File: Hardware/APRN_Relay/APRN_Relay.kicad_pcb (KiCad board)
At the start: 2 copper layers, 64 x 56 mm, 31 parts, among them J101 Pi_Zero, J102 SERVO1, J103 SERVO2, J104 PTT, J105 RADIO, J106 CHG_IN, U101 DHT11, U102 NCV1117ST50T3G

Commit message: Add text to the front (and ID for JLCPCB)
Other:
- board text added: "APRN Relay Board KW1FOX ${FULL_REVISION}"
- board text added: "JLCJLCJLCJLC"
- board text removed: "APRN Relay Board ${FULL_REVISION}"
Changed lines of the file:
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@@
   (gr_arc (start 100 153) (mid 97.87868 152.12132) (end 97 150) (layer "Edge.Cuts") (width 0.1))
   (gr_arc (start 161 150) (mid 160.12132 152.12132) (end 158 153) (layer "Edge.Cuts") (width 0.1))
-  (gr_text "APRN Relay Board\n${FULL_REVISION}" (at 100 136.5 90) (layer "F.SilkS")
-    (effects (font (size 1.5 1.5) (thickness 0.3)))
+  (gr_text "APRN Relay Board\nKW1FOX\n${FULL_REVISION}" (at 100.5 146.75 90) (layer "F.SilkS")
+    (effects (font (size 1.3 1.5) (thickness 0.3)) (justify left))
+  )
+  (gr_text "JLCJLCJLCJLC" (at 104.5 140.25 90) (layer "F.SilkS")
+    (effects (font (size 0.9 0.7) (thickness 0.175)))
   )
   (segment (start 142 151.515) (end 137 151.515) (width 0.4) (layer "F.Cu") (net 1))

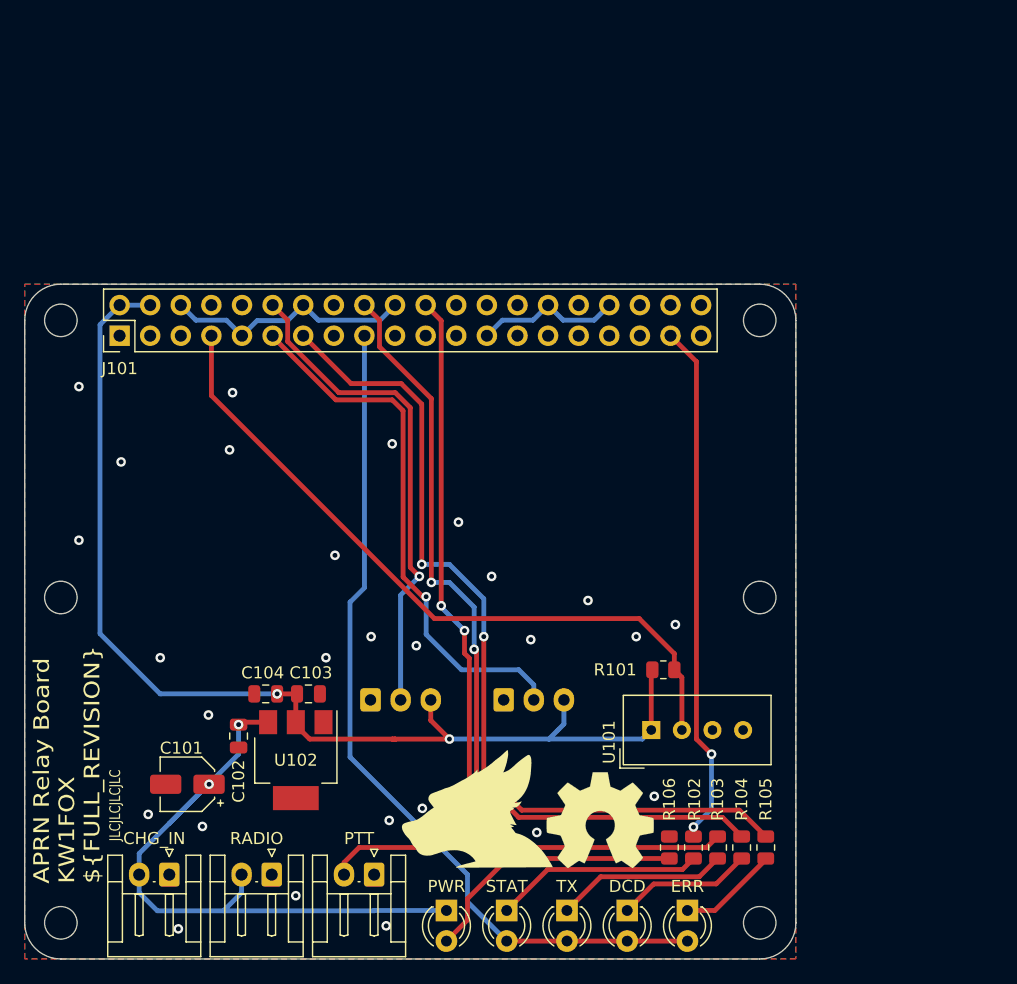
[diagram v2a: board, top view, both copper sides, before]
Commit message: Clean the last bits and prep for a tidy final review series, merge into 1.0 when done
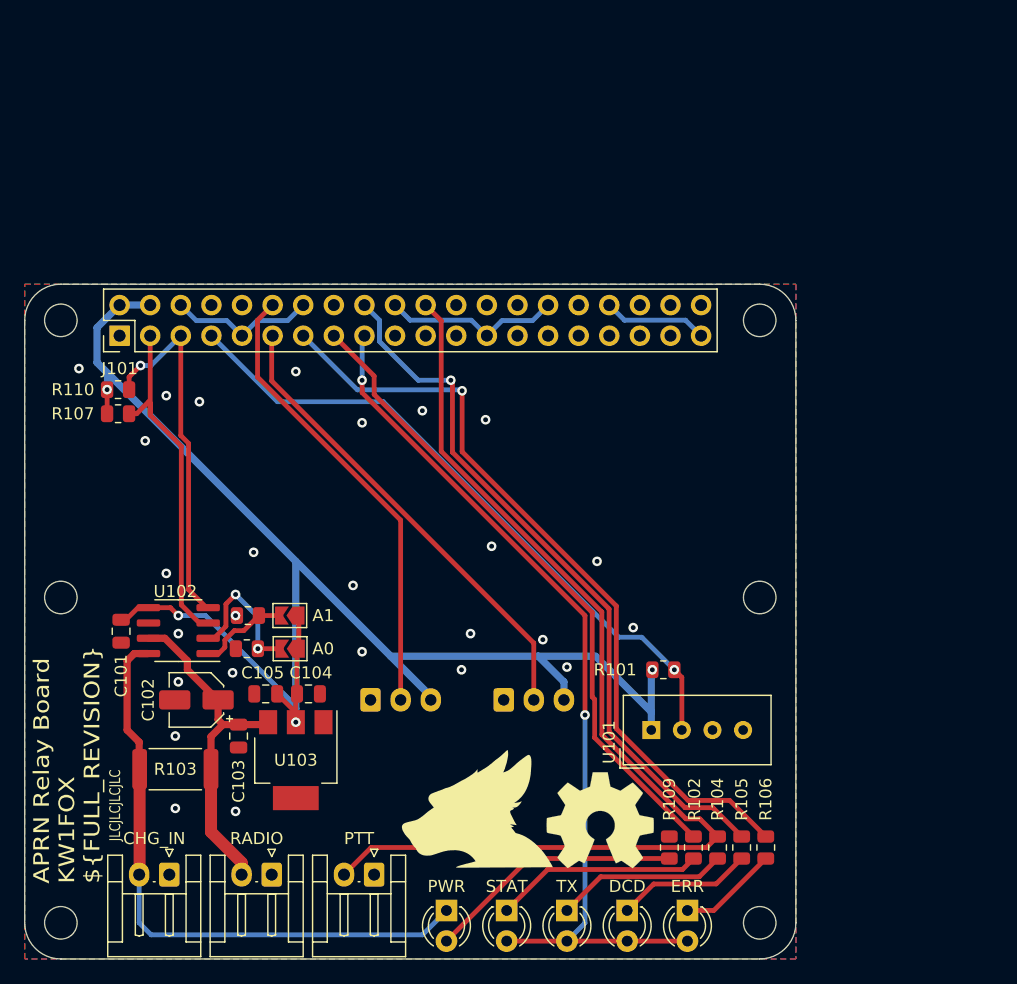
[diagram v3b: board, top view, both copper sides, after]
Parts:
- added C101: 1uF, Capacitor_SMD:C_0805_2012Metric, F.Cu at (105.0, 125.8)
- added JP101: A1, Jumper:SolderJumper-2_P1.3mm_Open_TrianglePad1.0x1.5mm, F.Cu at (119.0, 124.5)
- added JP102: A0, Jumper:SolderJumper-2_P1.3mm_Open_TrianglePad1.0x1.5mm, F.Cu at (119.0, 127.2)
- added R103: 100R, Resistor_SMD:R_2512_6332Metric, F.Cu at (109.5, 137.2)
- added R107: 10k, Resistor_SMD:R_0805_2012Metric, F.Cu at (104.8, 107.8)
- added R108: 10k, Resistor_SMD:R_0805_2012Metric, F.Cu at (115.5, 124.5)
- added R110: 10k, Resistor_SMD:R_0805_2012Metric, F.Cu at (104.8, 105.8)
- added R111: 10k, Resistor_SMD:R_0805_2012Metric, F.Cu at (115.4, 127.2)
- added U102: INA219AIDR, Package_SO:SOIC-8_3.9x4.9mm_P1.27mm, F.Cu at (109.8, 125.8)
- moved C102 7.04 mm to (111.2, 131.5)
- renumbered C101 to C102, C102 to C103, C103 to C104, C104 to C105, R103 to R104, R104 to R105, R105 to R106, R106 to R109, U102 to U103
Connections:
- C102 pad 1: +12V -> /PWR_IN
- C103 pad 1: +12V -> /PWR_IN
- J101 pad 15: unconnected-(J101-Pad15) -> /STAT
- J101 pad 3: unconnected-(J101-Pad3) -> /SDA
- J101 pad 37: /STAT -> unconnected-(J101-Pad37)
- J101 pad 5: unconnected-(J101-Pad5) -> /SCL
- J105 pad 2: +12V -> /PWR_IN
- U103 pad 3: +12V -> /PWR_IN
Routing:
- net +5V: track 95.8 -> 127.9 mm, vias 2 -> 4
- net /SCL: track 0.00 -> 30.3 mm, vias 0 -> 1
- net /SDA: track 0.00 -> 29.5 mm
- net /PWR_IN: track 0.00 -> 28.3 mm
- net /A0: track 0.00 -> 12.1 mm, vias 0 -> 2
- net /STAT: track 43.6 -> 53.9 mm, vias 2 -> 0
- net /DCD: track 67.9 -> 60.0 mm, vias 2 -> 1
- net /A1: track 0.00 -> 7.71 mm
- net /ERR: track 71.8 -> 64.5 mm, vias 2 -> 1
- net /TX: track 80.4 -> 87.1 mm, vias 2 -> 0
- net /SERVO2: track 44.9 -> 39.3 mm, vias 1 -> 0
- net /DHT_DATA: track 58.9 -> 55.2 mm, vias 0 -> 1
- net +12V: track 54.3 -> 51.0 mm, vias 2 -> 0
- net /SERVO1: track 41.2 -> 38.2 mm, vias 1 -> 0
- net GND: track 33.2 -> 35.7 mm, vias 27 -> 26
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
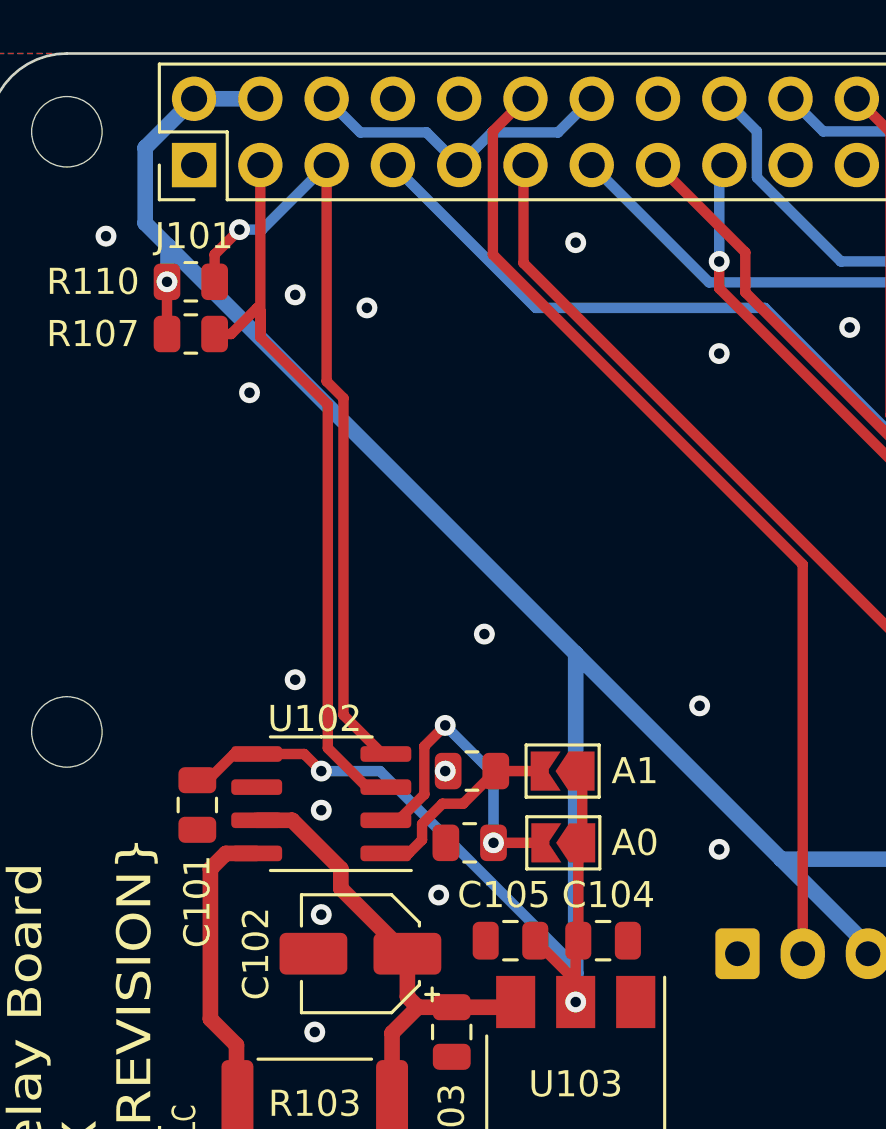
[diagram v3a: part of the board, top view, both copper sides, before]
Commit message: INA219 and I2C lines now driven by 3.3v instead of 5.0v
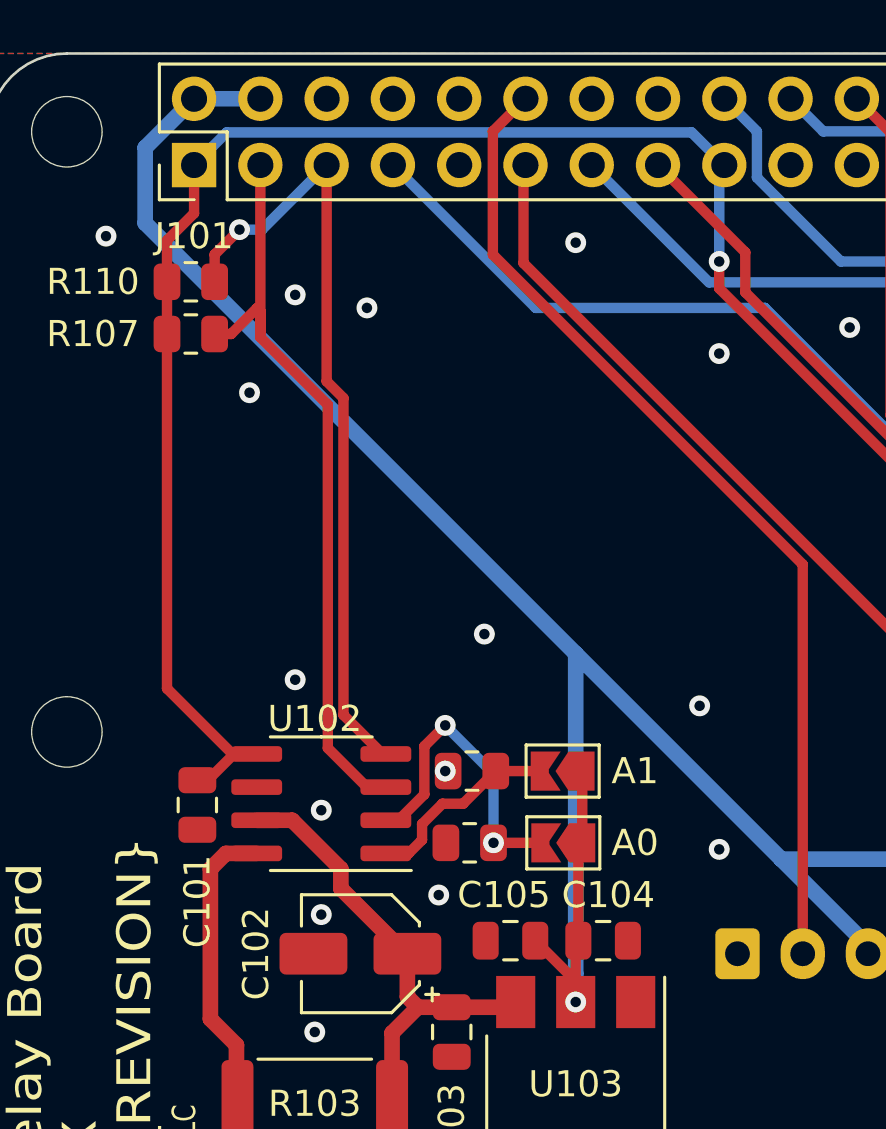
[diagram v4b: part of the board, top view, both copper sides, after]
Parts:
- R103: value 100R -> 0.1Ω
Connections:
- C101 pad 1: +5V -> +3V3
- J101 pad 1: unconnected-(J101-Pad1) -> +3V3
- J101 pad 14: GND -> unconnected-(J101-Pad14)
- J101 pad 6: GND -> unconnected-(J101-Pad6)
- R107 pad 2: +5V -> +3V3
- R110 pad 2: +5V -> +3V3
- U102 pad 5: +5V -> +3V3
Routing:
- net +3V3: track 73.6 -> 122.6 mm
- net +5V: track 127.9 -> 106.2 mm, vias 4 -> 2
- net GND: track 35.7 -> 23.5 mm

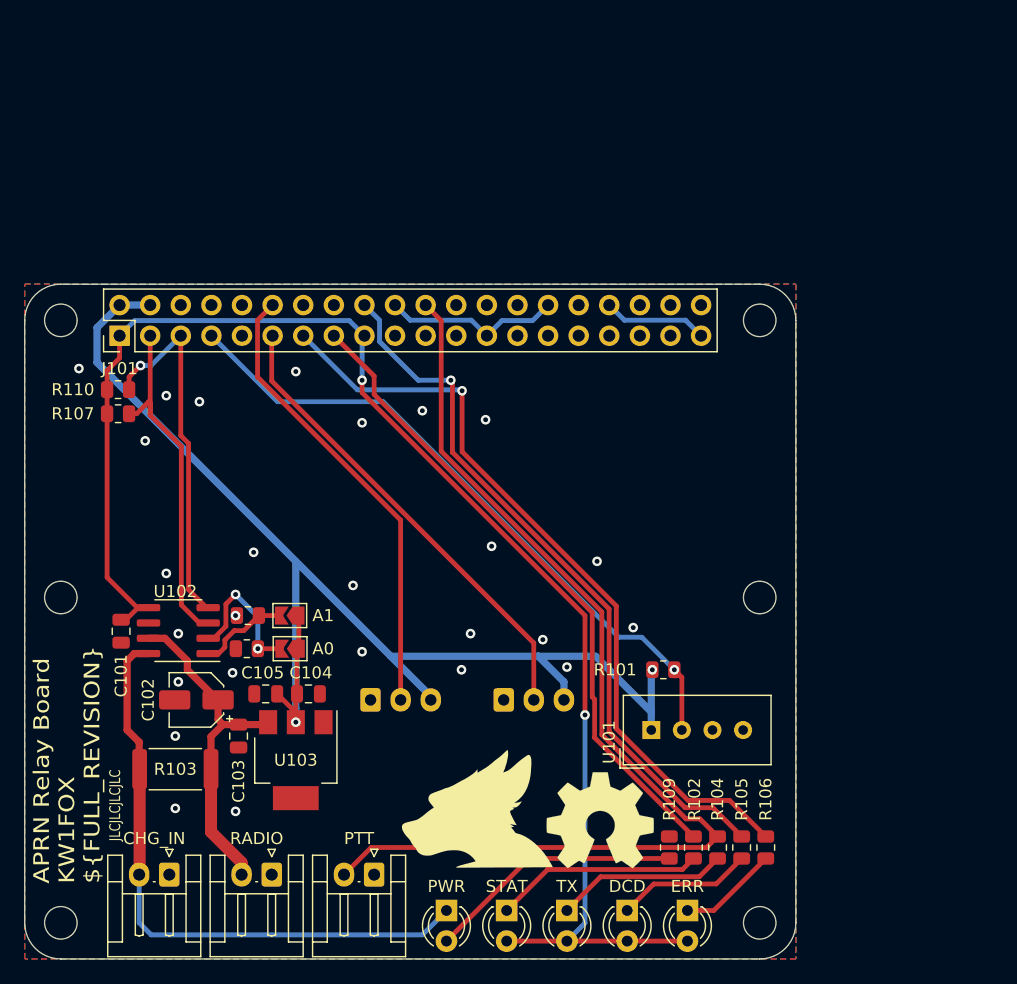
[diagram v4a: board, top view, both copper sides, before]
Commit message: Implement changes from dad
Co-Authored By: ka2qfx
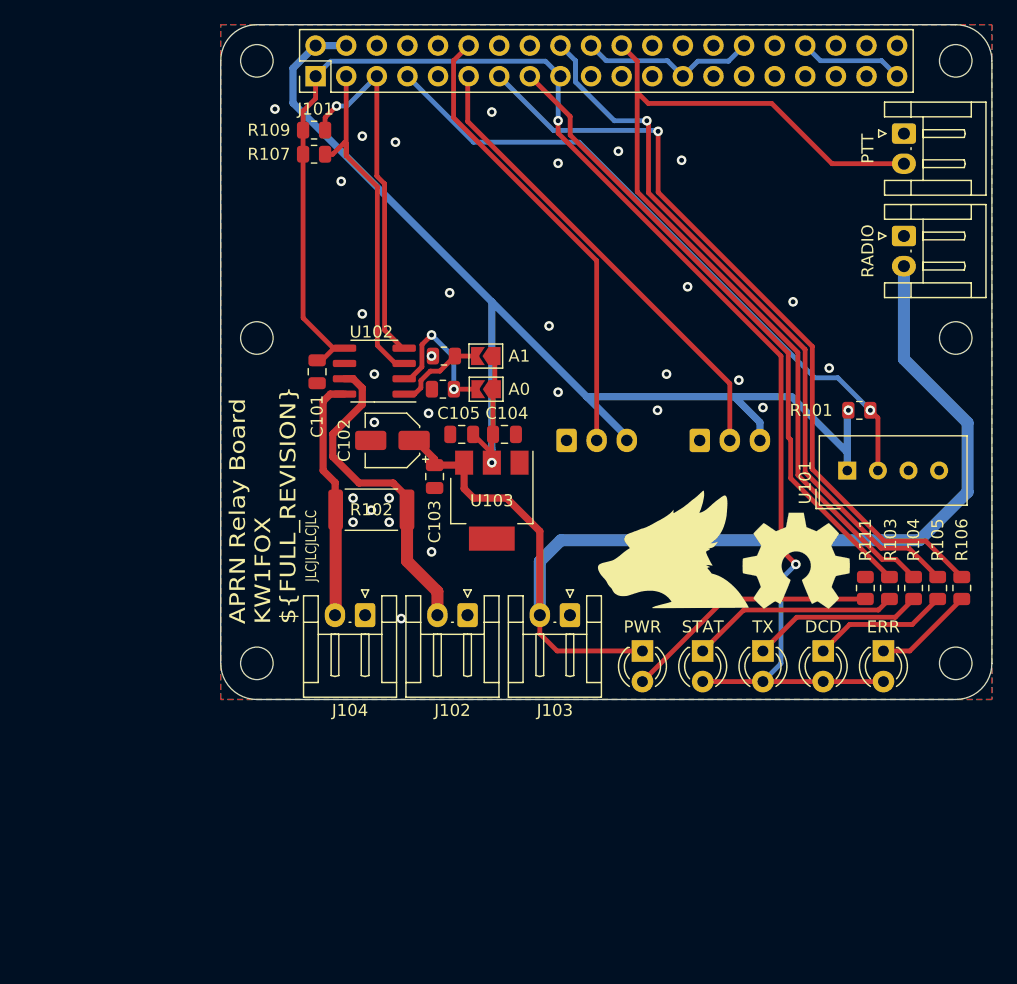
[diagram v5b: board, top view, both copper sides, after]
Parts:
- removed the J106 at (109.0, 146.0)
- added J102: CHG, Connector_JST:JST_EH_S2B-EH_1x02_P2.50mm_Horizontal, F.Cu at (133.8, 124.5)
- added J103: PWR, Connector_JST:JST_EH_S2B-EH_1x02_P2.50mm_Horizontal, F.Cu at (142.2, 124.5)
- added J104: BAT, Connector_JST:JST_EH_S2B-EH_1x02_P2.50mm_Horizontal, F.Cu at (125.2, 124.5)
- moved J107 75.6 mm to (170.0, 84.5), turned to -90 degrees
- moved J108 74.6 mm to (170.0, 93.0), turned to -90 degrees
- moved H106 27.0 mm to (174.3, 128.5)
- moved H103 27.0 mm to (116.3, 128.5)
- moved J101 27.0 mm to (121.1, 79.7)
- moved C103 27.0 mm to (131.0, 113.0)
- moved C105 27.0 mm to (133.3, 109.5)
- moved D101 27.0 mm to (153.3, 127.4)
- moved D102 27.0 mm to (158.3, 127.4)
- moved D103 27.0 mm to (163.3, 127.4)
- moved D104 27.0 mm to (168.3, 127.4)
- moved D105 27.0 mm to (148.3, 127.4)
- moved G*** 27.0 mm to (150.8, 119.0)
- moved H102 27.0 mm to (174.3, 78.5)
- moved H105 27.0 mm to (174.3, 101.5)
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- renumbered J102 to J105, J103 to J106, J104 to J107, J105 to J108, R103 to R102, R102 to R103, R110 to R109, R111 to R110, R109 to R111
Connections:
- C102 pad 1: /PWR_IN -> /POWER
- C103 pad 1: /PWR_IN -> /POWER
- D105 pad 1: +12V -> /POWER
- J108 pad 2: /PWR_IN -> /POWER
- R102 pad 1: /PWR_IN -> /CHARGE
- R102 pad 2: +12V -> /BATTERY
- U102 pad 7: /PWR_IN -> /CHARGE
- U102 pad 8: +12V -> /BATTERY
- U103 pad 3: /PWR_IN -> /POWER
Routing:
- net /POWER: track 0.00 -> 96.2 mm
- net +12V: track 51.0 -> 0.00 mm
- net /PWR_IN: track 28.3 -> 0.00 mm
- net /CHARGE: track 0.00 -> 26.9 mm
- net /BATTERY: track 0.00 -> 20.2 mm
- net /TX: track 87.1 -> 79.4 mm
- net +3V3: track 122.6 -> 123.6 mm
- net GND: vias 26 -> 30

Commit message: Include last changes from dad, thanks!
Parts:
- added JP101: PWR_BYPAS, Jumper:SolderJumper-2_P1.3mm_Open_TrianglePad1.0x1.5mm, B.Cu at (135.3, 121.0)
- R103, R104, R105, R106: value 270R -> 330R
- moved R111 17.6 mm to (149.2, 123.8), turned to 180 degrees
- moved R103 14.6 mm to (154.2, 123.8), turned to 180 degrees
- moved R104 11.6 mm to (159.2, 123.8), turned to 180 degrees
- moved R105 8.65 mm to (164.2, 123.8), turned to 180 degrees
- moved R106 5.73 mm to (169.2, 123.8), turned to 180 degrees
- moved G*** 4.44 mm to (147.2, 116.2)
- moved REF** 4.44 mm to (157.5, 117.2)
- moved C101 1.27 mm to (120.5, 103.2)
- turned R102 to 0 degrees
- renumbered J105 to J101, J106 to J102, J107 to J103, J101 to J104, J108 to J105, J102 to J106, J103 to J107, J104 to J108, JP101 to JP102, JP102 to JP103
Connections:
- D101 pad 2: +3V3 -> /STAT
- D102 pad 2: +3V3 -> /TX
- D103 pad 2: +3V3 -> /DCD
- D104 pad 2: +3V3 -> /ERR
- D105 pad 1: /POWER -> Net-(R111-Pad2)
- D105 pad 2: Net-(D105-Pad2) -> /POWER
- R102 pad 1: /CHARGE -> /BATTERY
- R102 pad 2: /BATTERY -> /CHARGE
- R103 pad 1: /STAT -> GND
- R104 pad 1: /TX -> GND
- R105 pad 1: /DCD -> GND
- R106 pad 1: /ERR -> GND
- R111 pad 2: Net-(D105-Pad2) -> Net-(R111-Pad2)
- U102 pad 7: /CHARGE -> /BATTERY
- U102 pad 8: /BATTERY -> /CHARGE
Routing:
- net +3V3: track 123.6 -> 49.4 mm, vias 2 -> 0
- net Net-(D105-Pad2): track 21.3 -> 0.00 mm
- net /BATTERY: track 20.2 -> 36.2 mm
- net Net-(D101-Pad1): track 17.3 -> 3.72 mm
- net Net-(D102-Pad1): track 14.3 -> 3.72 mm
- net /STAT: track 53.9 -> 62.2 mm
- net Net-(D103-Pad1): track 11.3 -> 3.72 mm
- net /ERR: track 64.5 -> 71.4 mm
- net /DCD: track 60.0 -> 66.1 mm
- net /TX: track 79.4 -> 85.0 mm
- net /POWER: track 96.2 -> 101.4 mm
- net Net-(D104-Pad1): track 8.29 -> 3.72 mm
- net Net-(R111-Pad2): track 0.00 -> 3.72 mm
- net /CHARGE: track 26.9 -> 26.0 mm
- net GND: vias 30 -> 36
